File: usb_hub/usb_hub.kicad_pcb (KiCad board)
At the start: 2 copper layers, 100 x 24 mm, 149 parts, among them Q1 2N3904, U1 TPS2044B, U10 USB_A_FEMALE, U11 USB_A_FEMALE, U12 SN75240, U13 SN75240, U14 M93C46, U15 USB_A_FEMALE, U16 USB_A_FEMALE, U17 USB_A_FEMALE, U18 USB_A_FEMALE, U2 TPS2044B, U3 TUSB2077A, U4 TPS76333, U5 USB_A_MALE, U6 SN75240, U7 SN75240, U8 SN75240, U9 USB_A_FEMALE, X1 6 MHz

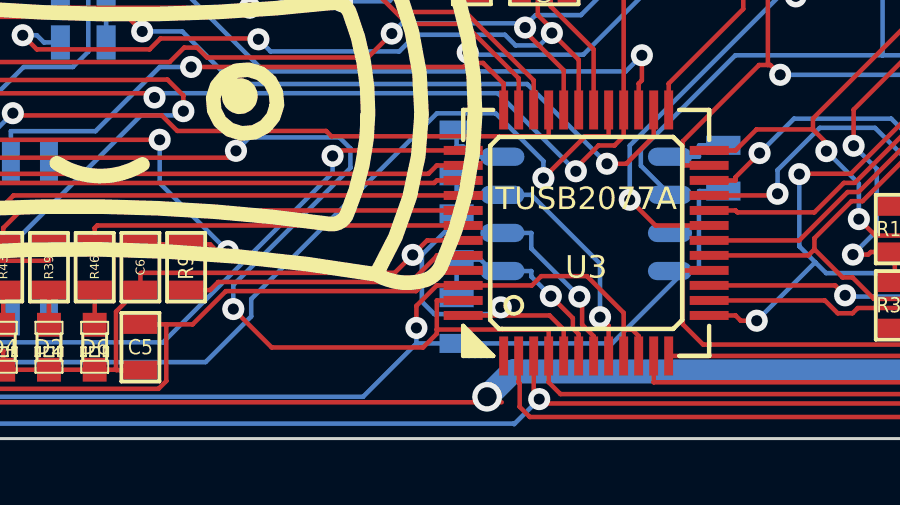
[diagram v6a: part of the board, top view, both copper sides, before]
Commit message: fixed pin 47 to gnd. need to clip and solder to adjacent pin
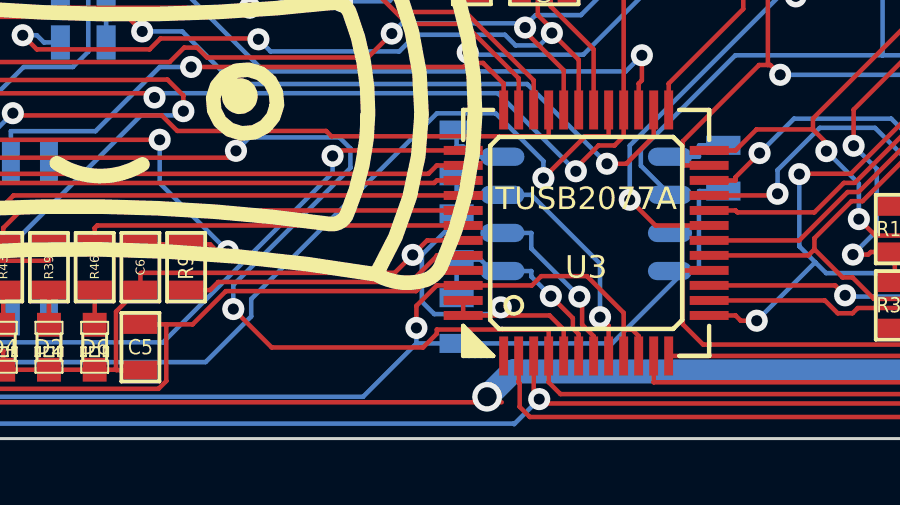
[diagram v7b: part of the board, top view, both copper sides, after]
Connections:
- U3 pad 47: DM0 -> GND
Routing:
- net DM0: track 87.8 -> 85.9 mm
- net GND: track 560.7 -> 561.2 mm

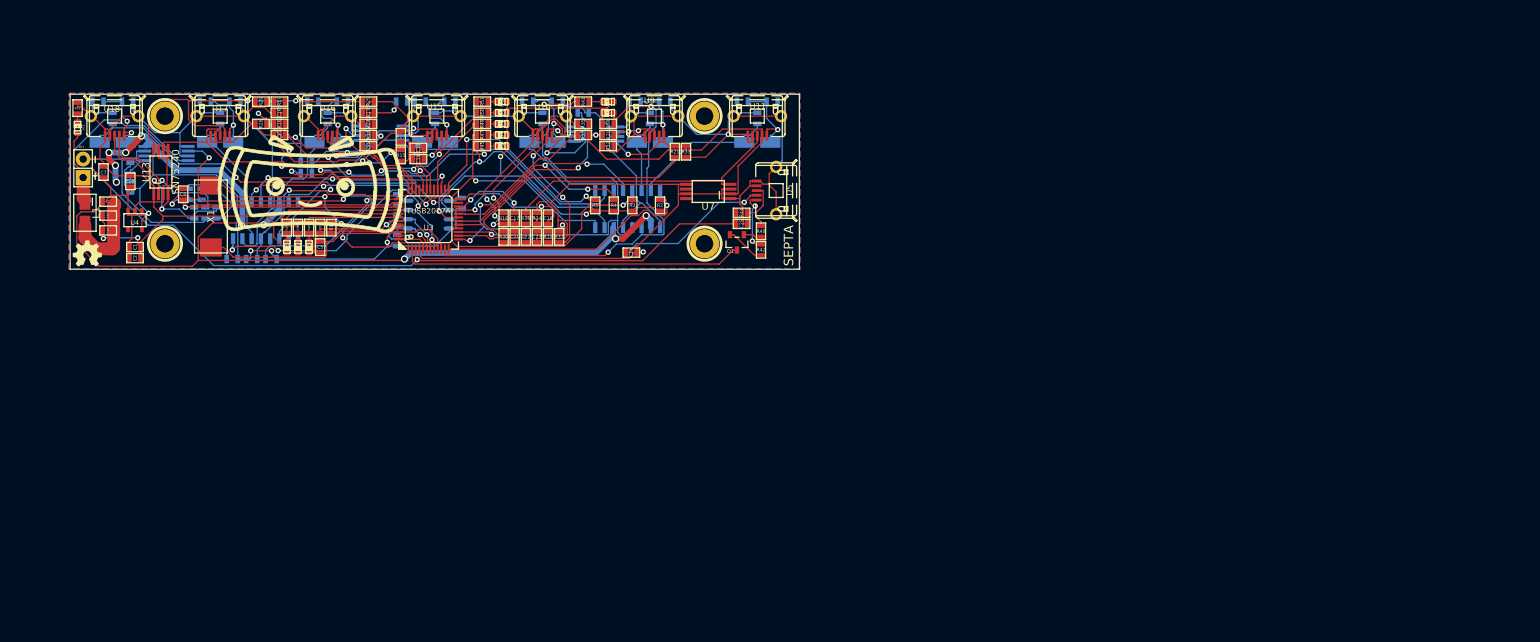
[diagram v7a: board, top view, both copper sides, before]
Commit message: Finished usb_hub revision B. Less complex, less that can go wrong
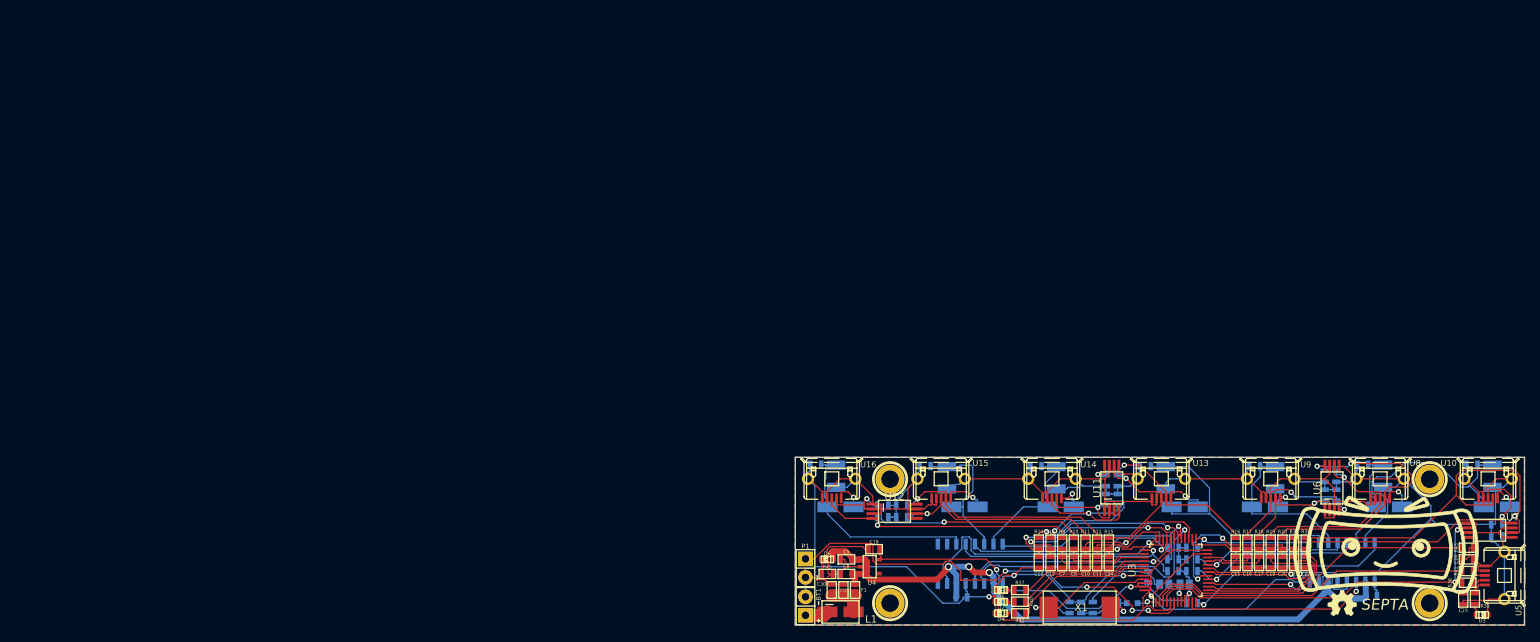
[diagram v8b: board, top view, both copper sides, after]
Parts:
- removed C41, C42, C43, C44: 22uF, SMD_Packages:SMD-0603
- removed C45, C46, C47, C48, C49: .1uF, SMD_Packages:SMD-0603
- removed D10, D11, D7, D8, D9: LED(G), LEDs:LED-0603
- removed G1: LOGO, usb_hub:oshw
- removed G2: LOGO, logo:logo
- removed Q1: 2N3904, Transistors_SMD:sot23
- removed R46, R47, R49, R50, R51, R52: 510, SMD_Packages:SMD-0603
- removed R48: 1.5k, SMD_Packages:SMD-0603
- removed R53: 1k, SMD_Packages:SMD-0603
- removed U17, U18: USB_A_FEMALE, ab2_usb:AB2_USB_MICRO_SMD
- added G***: LOGO, usb_hub:oshw, F.Cu at (210.0, 99.0)
- added G***: LOGO, usb_hub:LOGO, F.Cu at (216.0, 91.0)
- added JP1: JUMPER, Connect:GS2, B.Cu at (185.6, 96.4)
- added JP2: JUMPER, Connect:GS2, B.Cu at (188.4, 96.4)
- added P1: CONN_01X02, Pin_Headers:Pin_Header_Straight_1x02, F.Cu at (136.4, 94.2)
- C1, C2, C5, R2, R24, R25, R27, R28, R29, R3, R30, R31, R32, R33, R34, R4, R5: moved to B.Cu
- C10: value .1uF -> 22pF
- C12, U12, U6: moved to F.Cu
- C19: value 22pF -> 4.7uF; moved to F.Cu
- C20: value 4.7uF -> 22pF; moved to F.Cu
- C25: value 22pF -> 100uF; footprint SMD_Packages:SMD-0603 -> SMD_Packages:SMD-1210; moved to B.Cu
- C26: value 4.7uF -> 100uF; footprint SMD_Packages:SMD-0603 -> SMD_Packages:SMD-1210
- C27, C28, C37, C38, C39, C40: value 4.7uF -> .1uF
- C29: value .1uF -> 100uF; footprint SMD_Packages:SMD-0603 -> SMD_Packages:SMD-1210; moved to B.Cu
- C30: value 22uF -> .1uF; moved to F.Cu
- C31: value 22uF -> .1uF
- C33, C34, C36: value .1uF -> 100uF; footprint SMD_Packages:SMD-0603 -> SMD_Packages:SMD-1210
- C35: value 22uF -> 100uF; footprint SMD_Packages:SMD-0603 -> SMD_Packages:SMD-1210
- C4: value .1uF -> 33pF
- C6: value 33pF -> 4.7uF
- C7: value 4.7uF -> 22pF
- C9: value 22pF -> .1uF; moved to F.Cu
- D3: value LED(G) -> LED
- D5: value LED(G) -> LED; moved to B.Cu
- R10, R11, R14: value 30 -> 27; moved to F.Cu
- R12, R13, R15, R16, R17, R18, R19, R20, R36: value 30 -> 27
- R21: value 30 -> 15k; moved to B.Cu
- R35: value 15k -> 27
- R37: value 30 -> 510
- R38, R41: value 510 -> 27
- R40: value 30 -> 510; moved to F.Cu
- R42: value 15k -> 510
- R43: value 510 -> 1.5k
- R44: value 30 -> 510; moved to B.Cu
- R8: value 15k -> 1.5k
- R9: value 1.5k -> 27
- U1, U2: footprint Housings_SOIC:SOIC-16_Narrow -> Housings_SOIC:SOIC-16_3.9x9.9mm_Pitch1.27mm
- U11: value USB_A_FEMALE -> SN75240; footprint ab2_usb:AB2_USB_MICRO_SMD -> usb_hub:TSSOP8
- U13: value SN75240 -> USB_A_FEMALE; footprint usb_hub:TSSOP8 -> ab2_usb:AB2_USB_MICRO_SMD
- U14: value M93C46 -> USB_A_FEMALE; footprint Power_Integrations:SO-8 -> ab2_usb:AB2_USB_MICRO_SMD; moved to F.Cu
- U3: footprint Housings_QFP:lqfp-48 -> Housings_QFP:TQFP-48_7x7mm_Pitch0.5mm
- U8: value SN75240 -> USB_A_FEMALE; footprint usb_hub:TSSOP8 -> ab2_usb:AB2_USB_MICRO_SMD; moved to F.Cu
- moved C29 192.8 mm to (230.6, 81.6), turned to 90 degrees
- moved C1 176.2 mm to (214.0, 98.0)
- moved U8 171.6 mm to (215.2, 79.2), turned to 180 degrees
- moved R39 169.2 mm to (228.2, 98.4), turned to 90 degrees
- moved R43 167.8 mm to (227.2, 91.4), turned to 180 degrees
- moved C20 166.2 mm to (201.8, 93.4), turned to 270 degrees
- moved R29 157.0 mm to (209.2, 84.2), turned to 270 degrees
- moved C16 146.4 mm to (197.0, 93.4), turned to 270 degrees
- moved R17 145.9 mm to (197.0, 90.8), turned to 90 degrees
- moved C15 143.6 mm to (195.4, 93.4), turned to 270 degrees
- moved R16 143.2 mm to (195.4, 90.8), turned to 90 degrees
- moved U13 142.7 mm to (185.2, 79.2), turned to 180 degrees
- moved C4 142.2 mm to (172.6, 99.6), turned to 90 degrees
- moved C7 141.9 mm to (171.6, 93.4), turned to 270 degrees
- moved C10 141.0 mm to (174.8, 93.4), turned to 270 degrees
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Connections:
- C10 pad 1: VCC -> Net-(C10-Pad1)
- C19 pad 1: Net-(C19-Pad1) -> 3.3V
- C20 pad 1: 3.3V -> Net-(C20-Pad1)
- C23 pad 1: Net-(C23-Pad1) -> DM0
- C24 pad 1: DM0 -> DP0
- C25 pad 1: DP0 -> GND
- C25 pad 2: GND -> OUT2
- C26 pad 2: OUT2 -> OUT3
- C27 pad 2: OUT3 -> OUT2
- C28 pad 2: OUT1 -> OUT3
- C29 pad 1: Net-(C29-Pad1) -> GND
- C29 pad 2: GND -> OUT1
- C3 pad 1: RST -> 3.3V
- C30 pad 1: GND -> Net-(C30-Pad1)
- C30 pad 2: Net-(C30-Pad2) -> GND
- C31 pad 2: Net-(C31-Pad2) -> OUT1
- C32 pad 1: Net-(C29-Pad1) -> Net-(C30-Pad1)
- C33 pad 2: Net-(C30-Pad2) -> OUT4
- C34 pad 2: Net-(C31-Pad2) -> OUT5
- C35 pad 2: Net-(C35-Pad2) -> OUT6
- C36 pad 2: Net-(C35-Pad2) -> OUT7
- C4 pad 1: 3.3V -> Net-(C4-Pad1)
- C6 pad 1: Net-(C6-Pad1) -> VCC
- C7 pad 1: VCC -> Net-(C7-Pad1)
- C9 pad 1: Net-(C9-Pad1) -> VCC
- D1 pad 1: 3.3V -> Net-(D1-Pad1)
- D1 pad 2: Net-(D1-Pad2) -> GND
- D3 pad 1: 3.3V -> Net-(D3-Pad1)
- D3 pad 2: Net-(D3-Pad2) -> GND
- D5 pad 1: 3.3V -> Net-(D5-Pad1)
- D5 pad 2: Net-(D5-Pad2) -> SPND
- D6 pad 1: Net-(D6-Pad1) -> VCC
- D6 pad 2: GND -> Net-(D6-Pad2)
- F1 pad 1: Net-(C29-Pad1) -> Net-(C30-Pad1)
- L1 pad 2: Net-(C29-Pad1) -> Net-(C30-Pad1)
- L2 pad 1: OUT2 -> OUT3
- L2 pad 2: Net-(C30-Pad2) -> Net-(L2-Pad2)
- L3 pad 1: OUT3 -> OUT2
- L3 pad 2: Net-(C31-Pad2) -> Net-(L3-Pad2)
- L4 pad 2: Net-(C35-Pad2) -> Net-(L4-Pad2)
- L5 pad 2: Net-(C41-Pad2) -> Net-(L5-Pad2)
- L6 pad 2: Net-(C42-Pad2) -> Net-(L6-Pad2)
- L7 pad 2: Net-(C43-Pad2) -> Net-(L7-Pad2)
- L8 pad 2: Net-(C44-Pad2) -> Net-(L8-Pad2)
- R1 pad 2: RST -> OC1
- R10 pad 2: DP7 -> DM7
- R11 pad 1: Net-(C9-Pad1) -> Net-(C10-Pad1)
- R11 pad 2: DM7 -> DP6
- R12 pad 2: DP6 -> DM6
- R13 pad 2: DM6 -> DP5
- R14 pad 2: DP5 -> DM5
- R15 pad 2: DM5 -> DP4
- R16 pad 2: DP4 -> DM4
- R17 pad 2: DM4 -> DP3
- R18 pad 2: DP3 -> DM3
- R19 pad 2: DM3 -> DP2
- R2 pad 2: OC1 -> OC2
- R20 pad 1: Net-(C19-Pad1) -> Net-(C20-Pad1)
- R20 pad 2: DP2 -> DM2
- R21 pad 1: Net-(C21-Pad1) -> GND
- R21 pad 2: DM2 -> DP7
- R22 pad 2: DP7 -> DM7
- R23 pad 2: DM7 -> DP6
- R24 pad 2: DP6 -> DM6
- R25 pad 2: DM6 -> DP5
- R26 pad 2: DP5 -> DM5
- R27 pad 2: DM5 -> DP4
- R28 pad 2: DP4 -> DM4
- R29 pad 2: DM4 -> DP3
- R3 pad 2: OC2 -> OC3
- R30 pad 2: DP3 -> DM3
- R31 pad 2: DM3 -> DP2
- R32 pad 2: DP2 -> DM2
- R33 pad 2: DM2 -> DP1
- R34 pad 2: DP1 -> DM1
- R35 pad 1: GND -> Net-(C21-Pad1)
- R35 pad 2: DM1 -> DP1
- R36 pad 2: DP1 -> DM1
- R37 pad 1: Net-(C23-Pad1) -> HUBCFG
- R37 pad 2: DM1 -> Net-(D1-Pad1)
- R38 pad 1: Net-(D1-Pad2) -> Net-(R38-Pad1)
- R38 pad 2: PWRON1 -> DM0
- R39 pad 1: HUBCFG -> Net-(D3-Pad1)
- R39 pad 2: Net-(D2-Pad1) -> Net-(R39-Pad2)
- R4 pad 2: OC3 -> OC4
- R40 pad 1: Net-(R40-Pad1) -> PORTPWR
- R40 pad 2: DM0 -> Net-(D2-Pad1)
- R41 pad 1: Net-(D3-Pad2) -> Net-(R41-Pad1)
- R41 pad 2: PWRON2 -> DP0
- R42 pad 1: Net-(Q1-Pad2) -> PORTDIS
- R42 pad 2: Net-(R42-Pad2) -> Net-(D4-Pad1)
- R43 pad 1: PORTPWR -> DP0
- R43 pad 2: Net-(D4-Pad1) -> DP0PUR
- R44 pad 1: Net-(R44-Pad1) -> 3.3V
- R44 pad 2: DP0 -> Net-(D5-Pad1)
- R45 pad 1: Net-(D5-Pad2) -> GND
- R45 pad 2: PWRON3 -> Net-(D6-Pad2)
- R5 pad 2: OC4 -> OC5
- R6 pad 2: OC5 -> OC6
- R7 pad 2: OC6 -> OC7
- R8 pad 1: 3.3V -> Net-(R8-Pad1)
- R8 pad 2: OC7 -> Net-(C5-Pad1)
- R9 pad 1: Net-(R9-Pad1) -> Net-(C7-Pad1)
- R9 pad 2: Net-(C6-Pad1) -> DP7
- U10 pad 1: Net-(C31-Pad2) -> Net-(L4-Pad2)
- U10 pad 2: DM3 -> DM1
- U10 pad 3: DP3 -> DP1
- U11 pad 1: Net-(C35-Pad2) -> GND
- U11 pad 2: DM1 -> DM5
- U11 pad 3: DP1 -> GND
- U11 pad 4: GND -> DP5
- U11 pad 6: GND -> DP4
- U12 pad 2: DM5 -> DM7
- U12 pad 4: DP5 -> DP7
- U12 pad 6: DP4 -> DP6
- U12 pad 8: DM4 -> DM6
- U13 pad 1: GND -> Net-(L5-Pad2)
- U13 pad 2: DM7 -> DM4
- U13 pad 3: GND -> DP4
- U13 pad 4: DP7 -> GND
- U13 pad 6: DP6 -> GND
- U14 pad 1: RST -> Net-(L6-Pad2)
- U14 pad 2: EECLK -> DM5
- U14 pad 3: EEDATA -> DP5
- U14 pad 4: Net-(R53-Pad1) -> GND
- U14 pad 5: Net-(C49-Pad2) -> GND
- U14 pad 6: 3.3V -> GND
- U15 pad 1: Net-(C41-Pad2) -> Net-(L7-Pad2)
- U15 pad 2: DM4 -> DM6
- U15 pad 3: DP4 -> DP6
- U16 pad 1: Net-(C42-Pad2) -> Net-(L8-Pad2)
- U16 pad 2: DM5 -> DM7
- U16 pad 3: DP5 -> DP7
- U3 pad 1: Net-(U3-Pad1) -> SPND
- U3 pad 13: Net-(C23-Pad1) -> Net-(C22-Pad1)
- U3 pad 14: Net-(C22-Pad1) -> Net-(C21-Pad1)
- U3 pad 17: Net-(C21-Pad1) -> Net-(C20-Pad1)
- U3 pad 18: Net-(C19-Pad1) -> Net-(C18-Pad1)
- U3 pad 21: Net-(C18-Pad1) -> Net-(C17-Pad1)
- U3 pad 22: Net-(C17-Pad1) -> Net-(C16-Pad1)
- U3 pad 26: Net-(C16-Pad1) -> Net-(C15-Pad1)
- U3 pad 27: Net-(C15-Pad1) -> Net-(C14-Pad1)
- U3 pad 30: Net-(C14-Pad1) -> Net-(C13-Pad1)
- U3 pad 31: Net-(C13-Pad1) -> Net-(C12-Pad1)
- U3 pad 34: Net-(C12-Pad1) -> Net-(C11-Pad1)
- U3 pad 35: Net-(C11-Pad1) -> Net-(C10-Pad1)
- U3 pad 38: Net-(C9-Pad1) -> Net-(C8-Pad1)
- U3 pad 39: Net-(C8-Pad1) -> Net-(C7-Pad1)
- U3 pad 44: Net-(R9-Pad1) -> Net-(R8-Pad1)
- U3 pad 45: Net-(C5-Pad1) -> Net-(C4-Pad1)
- U3 pad 47: GND -> 3.3V
- U3 pad 7: EECLK -> Net-(U3-Pad7)
- U3 pad 8: EEDATA -> Net-(JP1-Pad2)
- U5 pad 1: Net-(R42-Pad2) -> Net-(R39-Pad2)
- U5 pad 2: Net-(R40-Pad1) -> Net-(R38-Pad1)
- U5 pad 3: Net-(R44-Pad1) -> Net-(R41-Pad1)
- U7 pad 6: Net-(U7-Pad6) -> DM0
- U7 pad 8: Net-(U7-Pad8) -> DP0
- U8 pad 1: GND -> Net-(L3-Pad2)
- U8 pad 2: 3.3V -> DM2
- U8 pad 3: GND -> DP2
- U8 pad 4: VCC -> GND
- U8 pad 6: DM0 -> GND
- U9 pad 1: Net-(C30-Pad2) -> Net-(L2-Pad2)
- U9 pad 2: DM2 -> DM3
- U9 pad 3: DP2 -> DP3
- X1 pad 1: Net-(C6-Pad1) -> Net-(C5-Pad1)
- X1 pad 2: Net-(C5-Pad1) -> Net-(C4-Pad1)
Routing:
- net GND: track 561.2 -> 460.0 mm, vias 7 -> 3
- net 3.3V: track 154.2 -> 68.3 mm, vias 6 -> 3
- net DP0: track 123.6 -> 51.5 mm, vias 1 -> 0
- net VCC: track 174.7 -> 120.9 mm, vias 10 -> 3
- net RST: track 7.40 -> 60.3 mm, vias 1 -> 4
- net Net-(C23-Pad1): track 41.9 -> 0.00 mm, vias 3 -> 0
- net Net-(C9-Pad1): track 36.7 -> 0.00 mm, vias 1 -> 0
- net PWRON2: track 57.4 -> 23.9 mm, vias 2 -> 1
- net PWRON1: track 59.0 -> 25.7 mm, vias 2 -> 1
- net DM0: track 85.9 -> 53.6 mm, vias 4 -> 2
- net Net-(C19-Pad1): track 30.5 -> 0.00 mm, vias 2 -> 0
- net Net-(C16-Pad1): track 36.0 -> 7.26 mm, vias 4 -> 0
- net DM2: track 12.1 -> 38.7 mm, vias 1 -> 2
- net Net-(C6-Pad1): track 23.9 -> 0.00 mm, vias 2 -> 0
- net Net-(C5-Pad1): track 29.9 -> 8.04 mm, vias 0 -> 1
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- added copper zone on F.Cu, net GND
- removed copper zone on F.Cu, net VCC
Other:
- board size 100 x 24 mm -> 100 x 23 mm
